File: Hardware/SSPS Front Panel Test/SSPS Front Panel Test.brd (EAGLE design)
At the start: 158.5 x 96.5 mm, 108 parts, among them J1 61400413321, SW1 B3W-9000-RG2C, SW2 B3W-9000-RG2C, SW3 5501M112, U1 P8X32A-M44, U10 STP16CP05XTTR, U11 CAT24C512WI-GT3, U12 IP4234CZ6, U13 FT234XD-R, U14 STP16CP05XTTR, U2 STP16CP05XTTR, U3 STP16CP05XTTR, U4 STP16CP05XTTR, U5 STP16CP05XTTR, U6 STP16CP05XTTR, U7 AP1084D25G-13, U8 AP1084D33G-13, U9 STP16CP05XTTR, X1 ABMM-6.000MHZ-B2-T

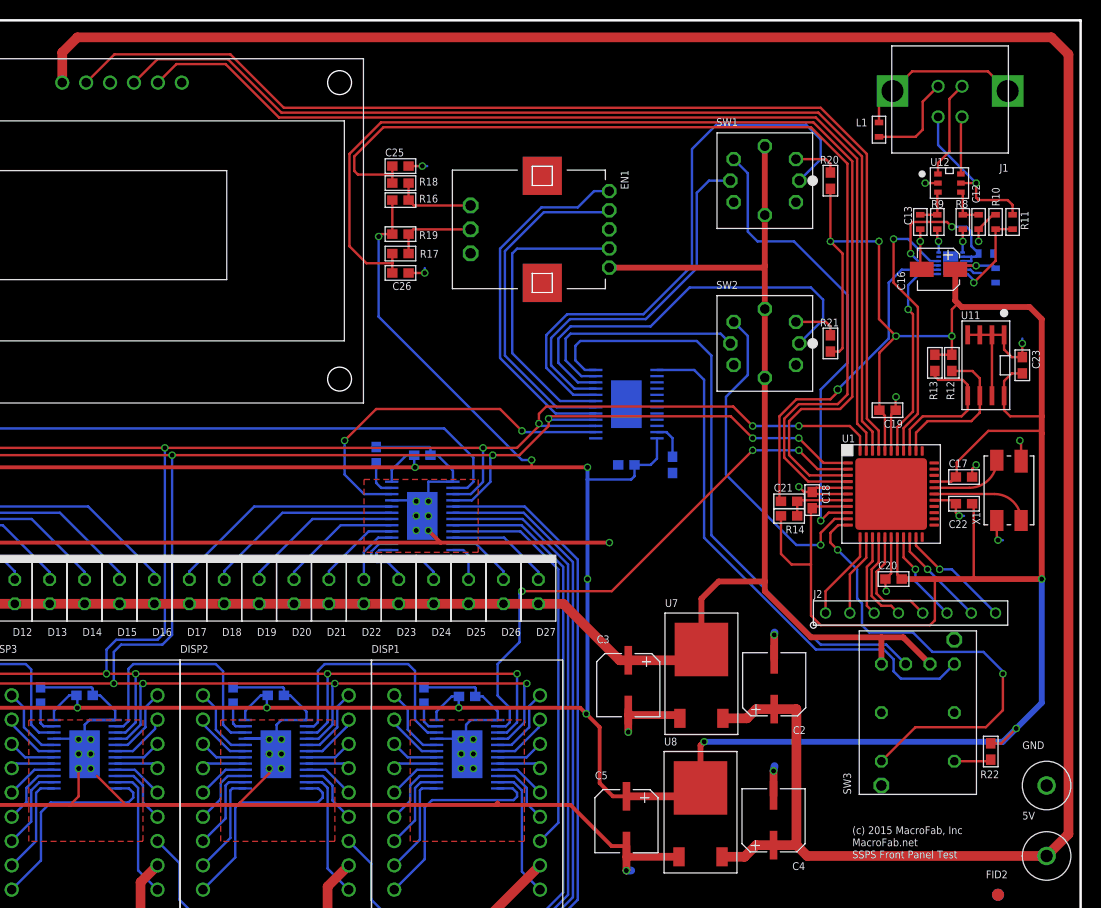
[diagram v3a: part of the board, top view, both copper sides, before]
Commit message: SSPS Front Panel Test fixed.
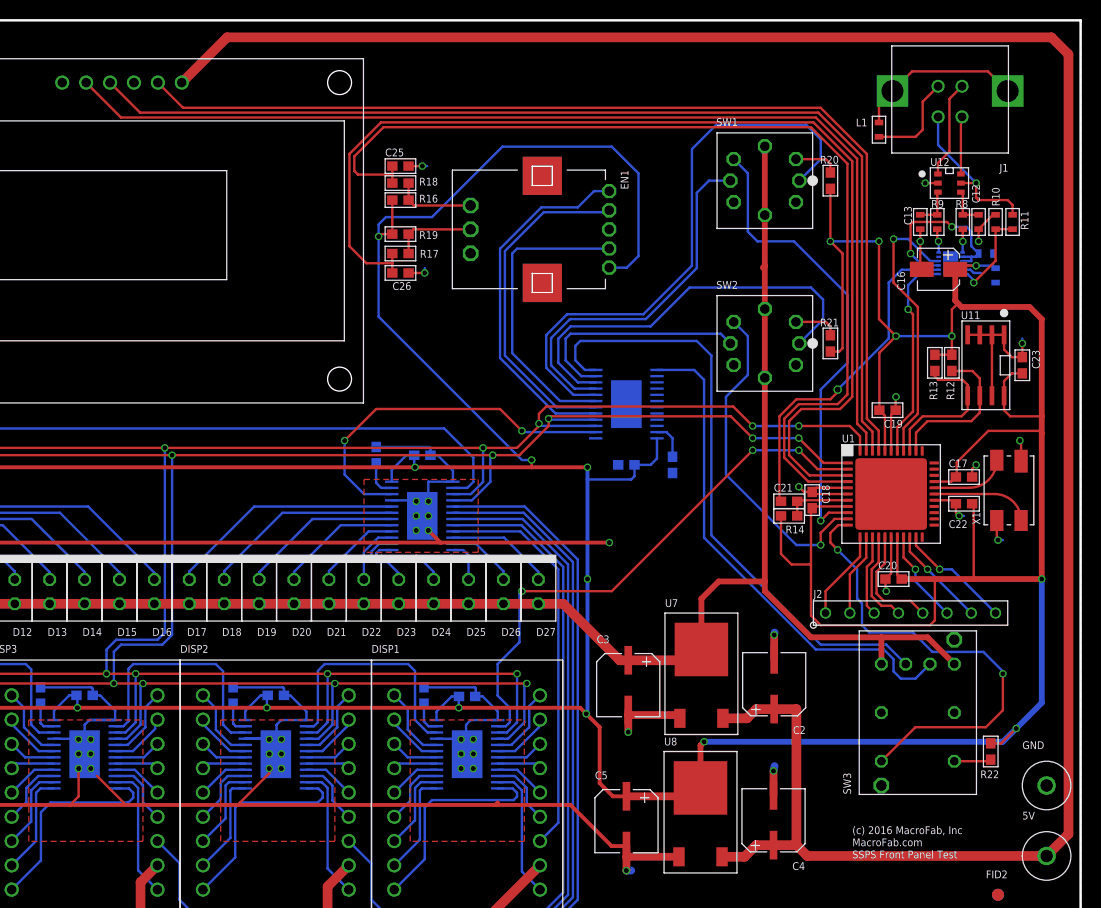
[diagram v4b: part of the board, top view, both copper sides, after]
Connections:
- net 2.5V: no longer EN1.5
- net 3.3V: now also EN1.5
- net GND: now also LCD1.P$18; no longer LCD1.P$17
- net LCD_SCK: now also LCD1.P$16; no longer LCD1.P$19
- net LCD_SI/SO: now also LCD1.P$19; no longer LCD1.P$16
- net LCD_STB: now also LCD1.P$17; no longer LCD1.P$18
- net VIN: now also LCD1.P$20; no longer LCD1.P$15
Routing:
- net 3.3V: track 554.8 -> 599.9 mm
- net VIN: track 251.7 -> 237.4 mm
- net 2.5V: track 371.1 -> 357.6 mm
- net LCD_SI/SO: track 118.7 -> 108.8 mm
- net LCD_SCK: track 109.0 -> 114.9 mm
- net N$48: track 55.5 -> 53.0 mm
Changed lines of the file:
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@@
 <element name="FRAME1" library="MF_Aesthetics" package="MF_FRAME_DEFAULT" value="MF_FRAMEDEFAULT" x="134.62" y="12.7">
 <attribute name="DNAME" value="PARKER DILLMANN" x="134.62" y="12.7" size="0.0508" layer="27" font="vector" display="off"/>
-<attribute name="REVNUM" value="REV: 1" x="134.62" y="12.7" size="0.0508" layer="27" font="vector" display="off"/>
+<attribute name="REVNUM" value="REV: 2" x="134.62" y="12.7" size="0.0508" layer="27" font="vector" display="off"/>
 </element>
 <element name="FID1" library="MF_Aesthetics" package="FIDUCIAL_100MIL" value="FIDUCIAL_100MIL" x="5.08" y="50.8"/>
@@
 <wire x1="142.748" y1="33.274" x2="143.256" y2="33.782" width="0.254" layer="1"/>
 <wire x1="143.256" y1="33.782" x2="143.256" y2="38.1" width="0.254" layer="1"/>
+<contactref element="EN1" pad="5"/>
+<wire x1="109.206" y1="70.66" x2="111.046" y2="70.66" width="0.254" layer="16"/>
+<wire x1="111.046" y1="70.66" x2="112.268" y2="71.882" width="0.254" layer="16"/>
+<wire x1="112.268" y1="71.882" x2="112.268" y2="80.518" width="0.254" layer="16"/>
+<wire x1="112.268" y1="80.518" x2="109.474" y2="83.312" width="0.254" layer="16"/>
+<wire x1="109.474" y1="83.312" x2="98.044" y2="83.312" width="0.254" layer="16"/>
+<wire x1="98.044" y1="83.312" x2="90.678" y2="75.946" width="0.254" layer="16"/>
+<wire x1="90.678" y1="75.946" x2="85.852" y2="75.946" width="0.254" layer="16"/>
+<wire x1="85.852" y1="75.946" x2="85.09" y2="75.184" width="0.254" layer="16"/>
+<wire x1="85.09" y1="75.184" x2="85.09" y2="73.914" width="0.254" layer="16"/>
 </signal>
 <signal name="GND">
@@
 <wire x1="138.088" y1="36.918" x2="138.176" y2="36.83" width="0.254" layer="1"/>
 <contactref element="GND" pad="P$1"/>
-<contactref element="LCD1" pad="P$17"/>
+<contactref element="LCD1" pad="P$18"/>
 <contactref element="U14" pad="P$1"/>
 <contactref element="U14" pad="PAD"/>
@@
 <wire x1="154.94" y1="9.144" x2="129.908" y2="9.144" width="1.016" layer="1"/>
 <wire x1="129.908" y1="9.144" x2="128.778" y2="10.274" width="1.016" layer="1"/>
-<contactref element="LCD1" pad="P$15"/>
-<wire x1="52.01" y1="90.008" x2="52.01" y2="93.158" width="1.016" layer="1"/>
-<wire x1="52.01" y1="93.158" x2="53.594" y2="94.742" width="1.016" layer="1"/>
-<wire x1="53.594" y1="94.742" x2="155.448" y2="94.742" width="1.016" layer="1"/>
+<contactref element="LCD1" pad="P$20"/>
 <wire x1="155.448" y1="94.742" x2="157.226" y2="92.964" width="1.016" layer="1"/>
 <wire x1="157.226" y1="92.964" x2="157.226" y2="11.43" width="1.016" layer="1"/>
 <wire x1="157.226" y1="11.43" x2="154.94" y2="9.144" width="1.016" layer="1"/>
+<wire x1="155.448" y1="94.742" x2="69.244" y2="94.742" width="1.016" layer="1"/>
+<wire x1="69.244" y1="94.742" x2="64.51" y2="90.008" width="1.016" layer="1"/>
 </signal>
 <signal name="2.5V">
@@
 <contactref element="SW3" pad="ANODE_1"/>
 <contactref element="SW2" pad="ANODE_2"/>
-<contactref element="EN1" pad="5"/>
 <wire x1="118.844" y1="30.734" x2="118.844" y2="36.04" width="0.6096" layer="1"/>
 <wire x1="118.844" y1="36.04" x2="120.65" y2="37.846" width="0.6096" layer="1"/>
 <wire x1="120.65" y1="37.846" x2="125.476" y2="37.846" width="0.6096" layer="1"/>
-<wire x1="137.668" y1="32.004" x2="139.954" y2="32.004" width="0.6096" layer="1"/>
-<wire x1="139.954" y1="32.004" x2="142.748" y2="29.21" width="0.6096" layer="1"/>
 <wire x1="137.668" y1="29.21" x2="137.668" y2="32.004" width="0.6096" layer="1"/>
 <wire x1="125.476" y1="59.138" x2="125.476" y2="37.846" width="0.6096" layer="1"/>
@@
 <wire x1="125.476" y1="70.866" x2="125.476" y2="76.156" width="0.6096" layer="1"/>
 <wire x1="125.476" y1="76.156" x2="125.476" y2="83.356" width="0.6096" layer="1"/>
-<wire x1="109.206" y1="70.66" x2="125.27" y2="70.66" width="0.6096" layer="1"/>
 <wire x1="125.27" y1="70.66" x2="125.476" y2="70.866" width="0.6096" layer="1"/>
 <wire x1="137.668" y1="32.004" x2="130.302" y2="32.004" width="0.6096" layer="1"/>
 <wire x1="130.302" y1="32.004" x2="125.476" y2="36.83" width="0.6096" layer="1"/>
 <wire x1="125.476" y1="36.83" x2="125.476" y2="37.846" width="0.6096" layer="1"/>
+<wire x1="145.288" y1="29.21" x2="142.494" y2="32.004" width="0.6096" layer="1"/>
+<wire x1="142.494" y1="32.004" x2="137.668" y2="32.004" width="0.6096" layer="1"/>
 </signal>
 <signal name="N$2">
@@
 </signal>
 <signal name="LCD_SI/SO">
-<contactref element="LCD1" pad="P$16"/>
+<contactref element="LCD1" pad="P$19"/>
 <contactref element="U1" pad="41"/>
 <wire x1="137.384" y1="51.49" x2="137.384" y2="53.624" width="0.254" layer="1"/>
@@
 <wire x1="136.144" y1="54.864" x2="136.144" y2="82.55" width="0.254" layer="1"/>
 <wire x1="136.144" y1="82.55" x2="131.318" y2="87.376" width="0.254" layer="1"/>
-<wire x1="131.318" y1="87.376" x2="75.184" y2="87.376" width="0.254" layer="1"/>
-<wire x1="75.184" y1="87.376" x2="69.596" y2="92.964" width="0.254" layer="1"/>
-<wire x1="69.596" y1="92.964" x2="57.466" y2="92.964" width="0.254" layer="1"/>
-<wire x1="57.466" y1="92.964" x2="54.51" y2="90.008" width="0.254" layer="1"/>
+<wire x1="131.318" y1="87.376" x2="64.642" y2="87.376" width="0.254" layer="1"/>
+<wire x1="64.642" y1="87.376" x2="62.01" y2="90.008" width="0.254" layer="1"/>
 </signal>
 <signal name="LCD_STB">
-<contactref element="LCD1" pad="P$18"/>
+<contactref element="LCD1" pad="P$17"/>
 <contactref element="U1" pad="42"/>
 <wire x1="136.734" y1="51.49" x2="136.734" y2="53.512" width="0.254" layer="1"/>
@@
 <wire x1="135.636" y1="54.61" x2="135.636" y2="82.296" width="0.254" layer="1"/>
 <wire x1="135.636" y1="82.296" x2="131.064" y2="86.868" width="0.254" layer="1"/>
-<wire x1="131.064" y1="86.868" x2="74.93" y2="86.868" width="0.254" layer="1"/>
-<wire x1="74.93" y1="86.868" x2="69.342" y2="92.456" width="0.254" layer="1"/>
-<wire x1="69.342" y1="92.456" x2="61.958" y2="92.456" width="0.254" layer="1"/>
-<wire x1="61.958" y1="92.456" x2="59.51" y2="90.008" width="0.254" layer="1"/>
+<wire x1="131.064" y1="86.868" x2="60.15" y2="86.868" width="0.254" layer="1"/>
+<wire x1="60.15" y1="86.868" x2="57.01" y2="90.008" width="0.254" layer="1"/>
 </signal>
 <signal name="LCD_SCK">
-<contactref element="LCD1" pad="P$19"/>
+<contactref element="LCD1" pad="P$16"/>
 <contactref element="U1" pad="43"/>
 <wire x1="136.084" y1="51.49" x2="136.084" y2="53.4" width="0.254" layer="1"/>
@@
 <wire x1="135.128" y1="54.356" x2="135.128" y2="82.042" width="0.254" layer="1"/>
 <wire x1="135.128" y1="82.042" x2="130.81" y2="86.36" width="0.254" layer="1"/>
-<wire x1="130.81" y1="86.36" x2="74.676" y2="86.36" width="0.254" layer="1"/>
-<wire x1="74.676" y1="86.36" x2="69.088" y2="91.948" width="0.254" layer="1"/>
-<wire x1="69.088" y1="91.948" x2="63.95" y2="91.948" width="0.254" layer="1"/>
-<wire x1="63.95" y1="91.948" x2="62.01" y2="90.008" width="0.254" layer="1"/>
+<wire x1="130.81" y1="86.36" x2="58.158" y2="86.36" width="0.254" layer="1"/>
+<wire x1="58.158" y1="86.36" x2="54.51" y2="90.008" width="0.254" layer="1"/>
 </signal>
 <signal name="N$39">
@@
 <wire x1="138.938" y1="29.718" x2="138.938" y2="28.448" width="0.254" layer="16"/>
 <wire x1="138.938" y1="28.448" x2="139.7" y2="27.686" width="0.254" layer="16"/>
-<wire x1="139.7" y1="27.686" x2="143.764" y2="27.686" width="0.254" layer="16"/>
-<wire x1="143.764" y1="27.686" x2="145.288" y2="29.21" width="0.254" layer="16"/>
+<wire x1="139.7" y1="27.686" x2="141.224" y2="27.686" width="0.254" layer="16"/>
+<wire x1="141.224" y1="27.686" x2="142.748" y2="29.21" width="0.254" layer="16"/>
 <wire x1="119.126" y1="42.418" x2="130.81" y2="30.734" width="0.254" layer="16"/>
 <wire x1="130.81" y1="30.734" x2="137.922" y2="30.734" width="0.254" layer="16"/>
